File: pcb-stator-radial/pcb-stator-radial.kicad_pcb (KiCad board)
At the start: 2 copper layers, 116 x 114.4 mm, 12 parts, among them J1 A+, J2 A-, J3 B+, J4 B-, J5 C+, J6 C-

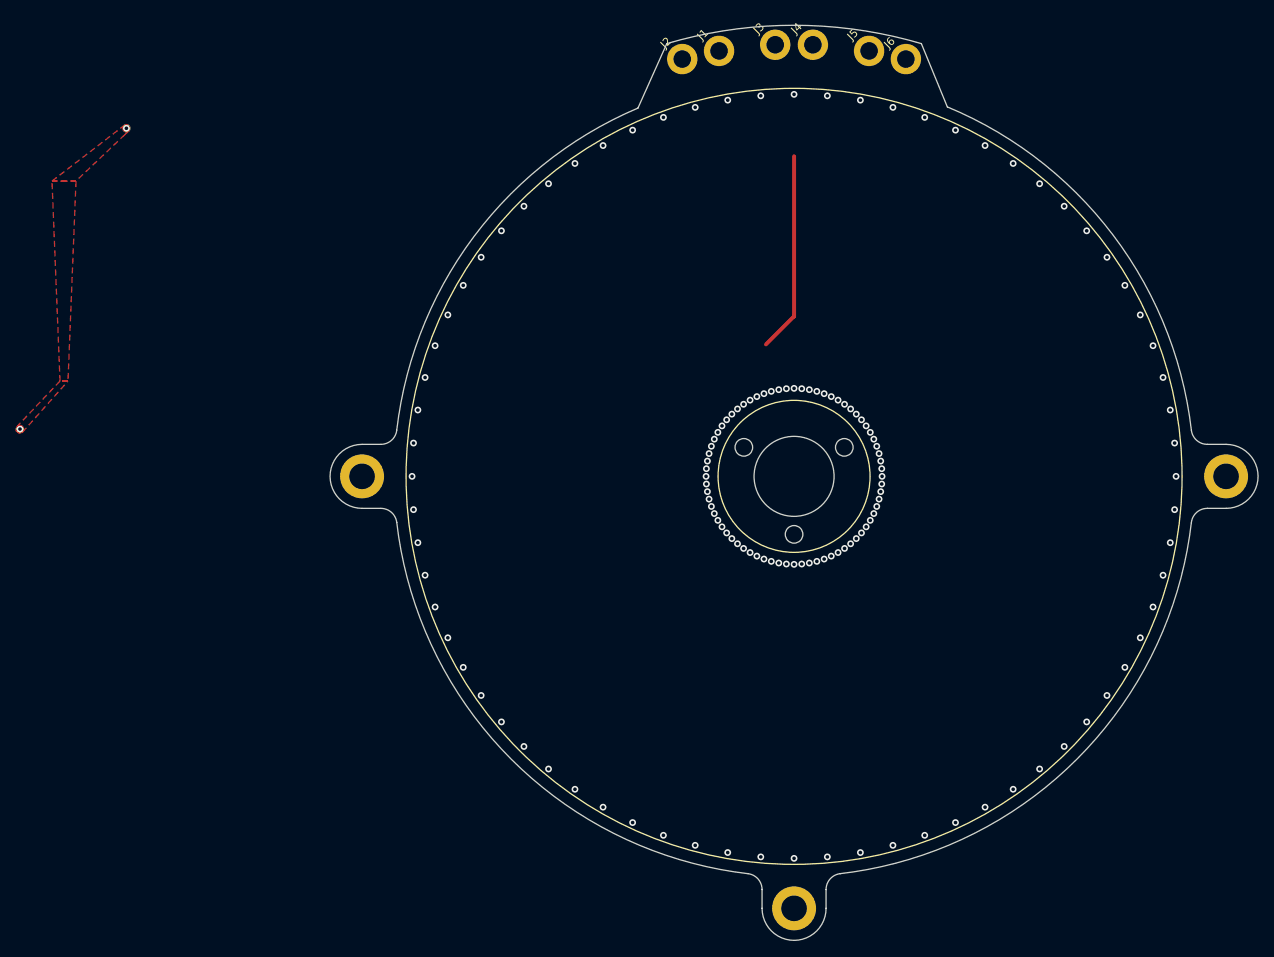
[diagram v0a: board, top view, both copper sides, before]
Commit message: Routed (96 slot, 16 pole)
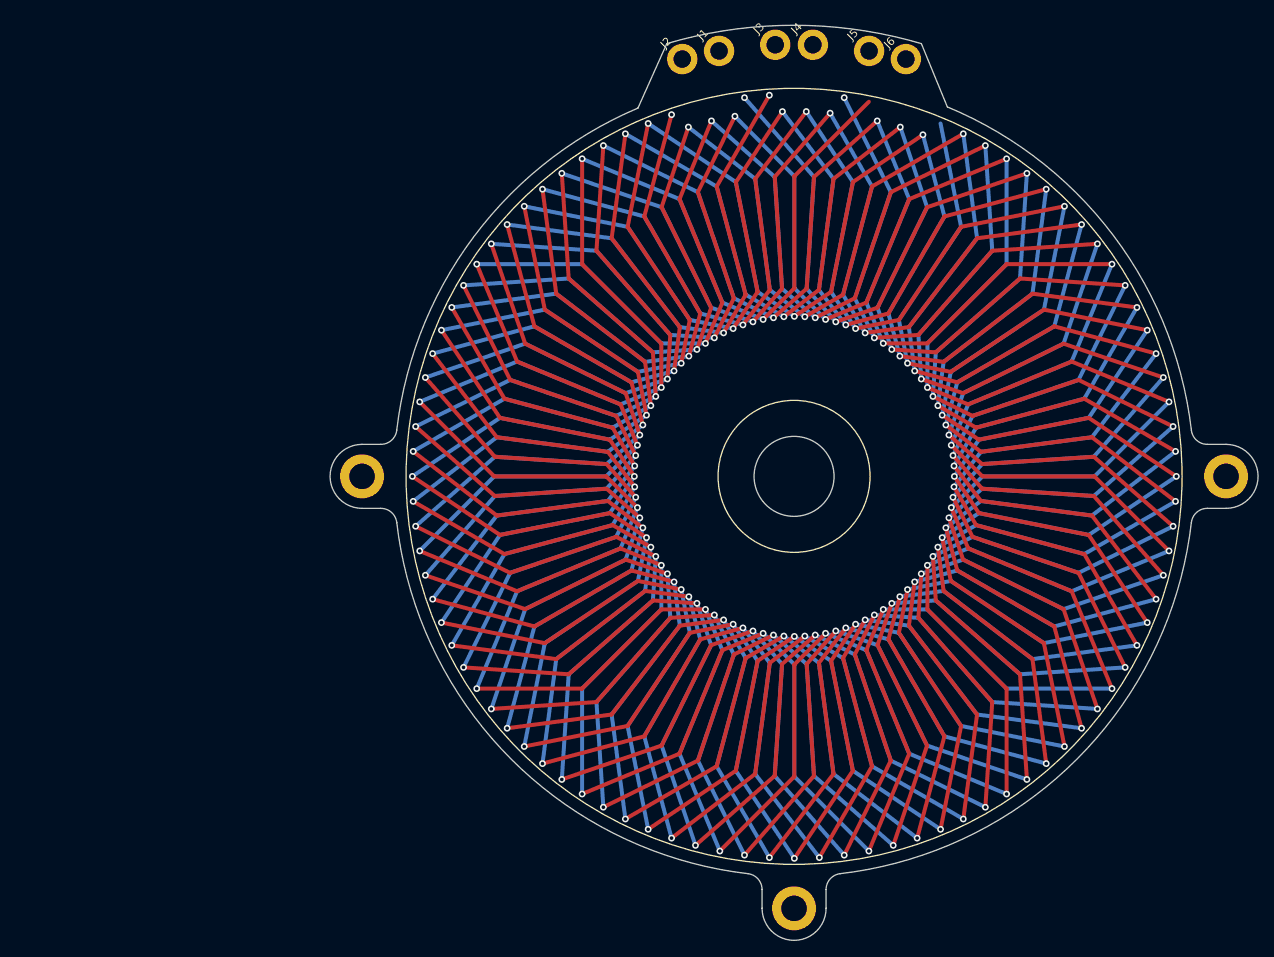
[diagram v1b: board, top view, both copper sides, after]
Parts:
- removed H4, H5, H6: MountingHole, MountingHole:MountingHole_2.2mm_M2_ISO14580
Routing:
- net /B_Phase: track 0.00 -> 2076.6 mm, vias 0 -> 65
- net /A_Phase: track 0.00 -> 2076.6 mm, vias 0 -> 63
- net /C_Phase: track 24.9 -> 2076.6 mm, vias 3 -> 65
- net (no net): vias 143 -> 0
- removed copper zone on B.Cu, net /C_Phase
- removed copper zone on F.Cu, net /C_Phase
